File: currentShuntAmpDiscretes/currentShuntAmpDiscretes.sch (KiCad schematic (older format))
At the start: 9 parts, among them Q1 2N3906, Q2 2N3906

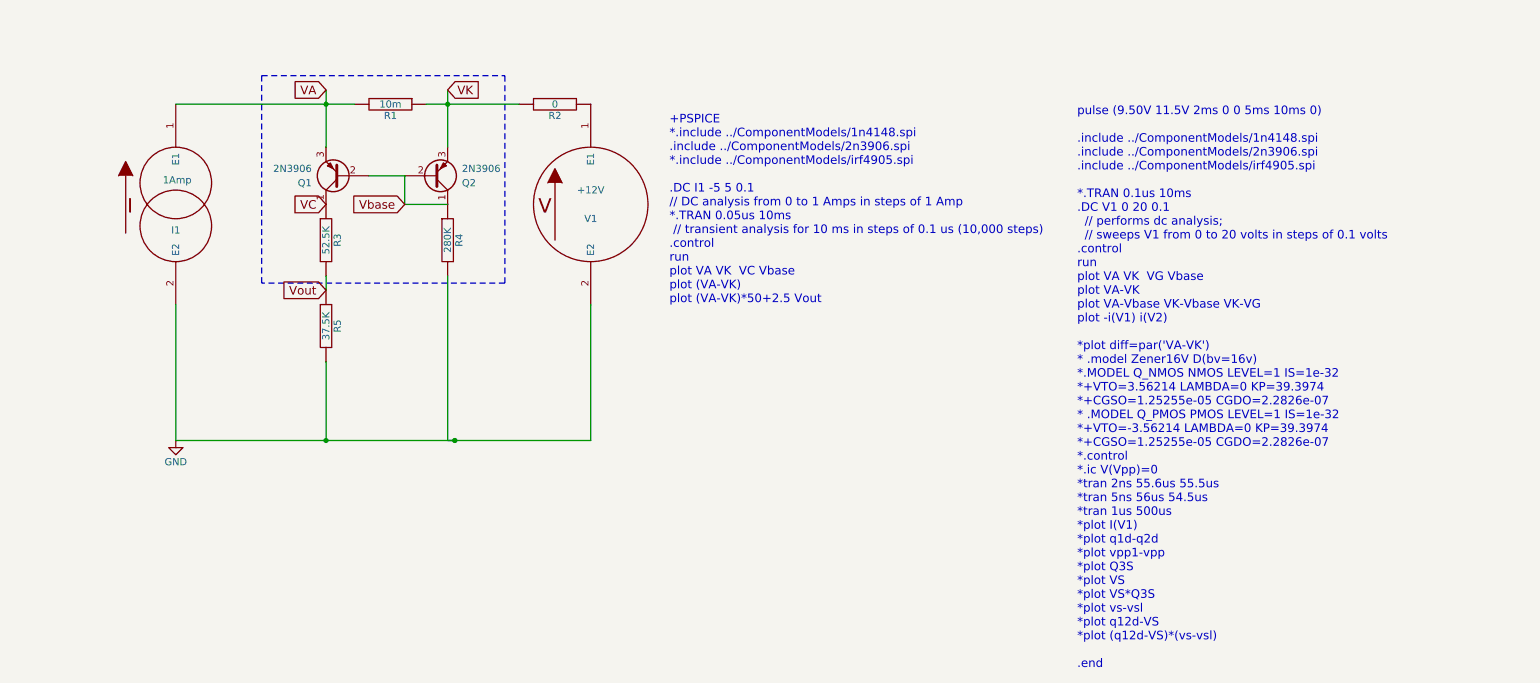
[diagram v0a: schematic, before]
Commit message: Update to current shunt amplifier and addition of new circuit with emitter resistors
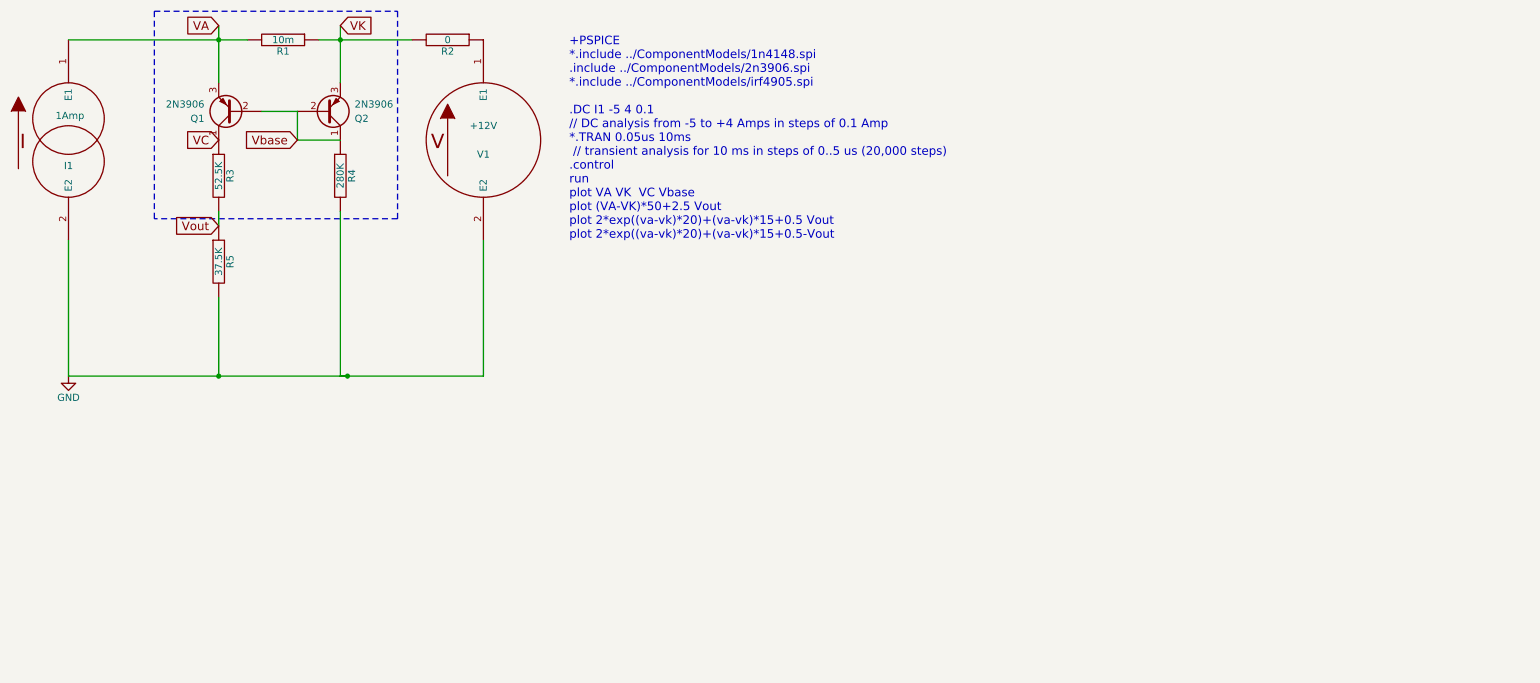
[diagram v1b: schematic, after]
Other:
- note added: "+PSPICE \n*.include ../ComponentModels/1n4148.spi\n.include ../ComponentModels/2n3906.spi\n*.include ../ComponentModels/irf4905.spi\n\n.DC I1 -5 4 0.1\n// DC analysis from -5 to +4 Amps in steps of 0.1 Amp\n*.TRAN 0.05us 10ms\n // transient analysis for 10 ms in steps of 0..5 us (20,000 steps)\n.control\nrun\nplot VA VK VC Vbase\nplot (VA-VK)*50+2.5 Vout\nplot 2*exp((va-vk)*20)+(va-vk)*15+0.5 Vou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"
- note removed: "+PSPICE \n*.include ../ComponentModels/1n4148.spi\n.include ../ComponentModels/2n3906.spi\n*.include ../ComponentModels/irf4905.spi\n\n.DC I1 -5 5 0.1\n// DC analysis from 0 to 1 Amps in steps of 1 Amp\n*.TRAN 0.05us 10ms\n // transient analysis for 10 ms in steps of 0.1 us (10,000 steps)\n.control\nrun\nplot VA VK VC Vbase\nplot (VA-VK)\nplot (VA-VK)*50+2.5 Vout"
- note removed: "pulse (9.50V 11.5V 2ms 0 0 5ms 10ms 0)\n\n.include ../ComponentModels/1n4148.spi\n.include ../ComponentModels/2n3906.spi\n.include ../ComponentModels/irf4905.spi\n\n*.TRAN 0.1us 10ms \n.DC V1 0 20 0.1\n // performs dc analysis; \n // sweeps V1 from 0 to 20 volts in steps of 0.1 volts\n.control\nrun\nplot VA VK VG Vbase\nplot VA-VK\nplot VA-Vbase VK-Vbase VK-VG\nplot -i(V1) i(V2)\n\n*plot diff=par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"
